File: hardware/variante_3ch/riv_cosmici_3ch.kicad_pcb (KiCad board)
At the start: 2 copper layers, 103 x 215 mm, 203 parts, among them J101 SiPM_CH1, J104 LEMO_CH1, J201 SiPM_CH2, J204 LEMO_CH2, J3 PWR_5V, J301 SiPM_CH3, J304 LEMO_CH3, J5 LEMO_AND, J6 I2C_RPI, Q101 BFR93A, Q102 MMBTH81, Q201 BFR93A, Q202 MMBTH81, Q301 BFR93A, Q302 MMBTH81, U1 LT3461, U10 74LVC1G11, U102 TLC555/LMC555, U103 MAX961, U108 LT1636, U109 74LVC1G17, U11 MCP3424, U202 TLC555/LMC555, U203 MAX961, U208 LT1636, U209 74LVC1G17, U302 TLC555/LMC555, U303 MAX961, U308 LT1636, U309 74LVC1G17, U5 LP2985AIM5-3.6, U6 MCP1825S-3302, U7 LP2985AIM5-3.6

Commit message: KiCad 10: nomi delle reti del PCB allineati allo schema, VOUT del LT3461 come uscita di alimentazione
- allinea_reti_kicad.py (chiamato da gen_variante3): le reti del PCB prendono i nomi
  che KiCad ricava dallo schema (/ETICHETTA, Net-(...), unconnected-(...)), dopo aver
  verificato che i collegamenti coincidono: elimina i 199 net_conflict del DRC con
  --schematic-parity.
- LT3461 pin 5 (CAP/VOUT) di tipo power_out: risolve l'unico power_pin_not_driven
  dell'ERC (VOUT40 alimenta i V+ dei tre LT1636).
Verifica KiCad su entrambe le schede: OK.

Co-Authored-By: Claude Opus 5.5 <noreply@anthropic.com>
Claude-Session: https://claude.ai/code/session_017fc9yPsNewCQrMK8R1c8Ls
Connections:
- net AND_IN1 renamed /AND_IN1
- net AND_IN2 renamed /AND_IN2
- net AND_IN3 renamed /AND_IN3
- net AND_OUT renamed /AND_OUT
- net AND_Y renamed /AND_Y
- net BIAS1 renamed /BIAS1
- net BIAS2 renamed /BIAS2
- net BIAS3 renamed /BIAS3
- net BUF_OUT1 renamed Net-(J104-Pad1)
- net BUF_OUT2 renamed Net-(J204-Pad1)
- net BUF_OUT3 renamed Net-(J304-Pad1)
- net BUF_Y1 renamed /BUF_Y1
- net BUF_Y2 renamed /BUF_Y2
- net BUF_Y3 renamed /BUF_Y3
- net CMP_IN1 renamed /CMP_IN1
- net CMP_IN2 renamed /CMP_IN2
- net CMP_IN3 renamed /CMP_IN3
- net CMP_Q1 renamed /CMP_Q1
- net CMP_Q2 renamed /CMP_Q2
- net CMP_Q3 renamed /CMP_Q3
- net CMP_QB1 renamed /CMP_QB1
- net CMP_QB2 renamed /CMP_QB2
- net CMP_QB3 renamed /CMP_QB3
- net CTL5551 renamed Net-(U102-CTL)
- net CTL5552 renamed Net-(U202-CTL)
- net CTL5553 renamed Net-(U302-CTL)
- net FB renamed Net-(U1-FB)
- net I2C_SCL renamed /I2C_SCL
- net I2C_SDA renamed /I2C_SDA
- net INV1 renamed Net-(U108--)
- net INV2 renamed Net-(U208--)
- net INV3 renamed Net-(U308--)
- net LE1 renamed Net-(U103-LE)
- net LE2 renamed Net-(U203-LE)
- net LE3 renamed Net-(U303-LE)
- net LED_A1 renamed Net-(U102-Q)
- net LED_A2 renamed Net-(U202-Q)
- net LED_A3 renamed Net-(U302-Q)
- net LED_K1 renamed Net-(D103-A)
- net LED_K2 renamed Net-(D203-A)
- net LED_K3 renamed Net-(D303-A)
- net MON1 renamed /MON1
- net MON2 renamed /MON2
- net MON3 renamed /MON3
- net MON4 renamed /MON4
- net Q1B1 renamed Net-(Q101-B)
- net Q1B2 renamed Net-(Q201-B)
- net Q1B3 renamed Net-(Q301-B)
- net Q1C1 renamed Net-(Q101-C)
- net Q1C2 renamed Net-(Q201-C)
- net Q1C3 renamed Net-(Q301-C)
- net Q2C1 renamed Net-(Q102-C)
- net Q2C2 renamed Net-(Q202-C)
- net Q2C3 renamed Net-(Q302-C)
- net Q2E1 renamed Net-(Q102-E)
- net Q2E2 renamed Net-(Q202-E)
- net Q2E3 renamed Net-(Q302-E)
- net SCL_ADC renamed /SCL_ADC
- net SDA_ADC renamed /SDA_ADC
- net SIG_IN1 renamed /SIG_IN1
- net SIG_IN2 renamed /SIG_IN2
- net SIG_IN3 renamed /SIG_IN3
- net SW renamed Net-(U1-SW)
- net T5551 renamed Net-(U102-DIS)
- net T5552 renamed Net-(U202-DIS)
- net T5553 renamed Net-(U302-DIS)
- net TH1 renamed /TH1
- net TH2 renamed /TH2
- net TH3 renamed /TH3
- net TH_HI1 renamed Net-(R119-Pad1)
- net TH_HI2 renamed Net-(R219-Pad1)
- net TH_HI3 renamed Net-(R319-Pad1)
- net TH_LO1 renamed Net-(R118-Pad1)
- net TH_LO2 renamed Net-(R218-Pad1)
- net TH_LO3 renamed Net-(R318-Pad1)
- net TH_W1 renamed Net-(V102-W)
- net TH_W2 renamed Net-(V202-W)
- net TH_W3 renamed Net-(V302-W)
- net VADJ_HI1 renamed Net-(D101-K)
- net VADJ_HI2 renamed Net-(D201-K)
- net VADJ_HI3 renamed Net-(D301-K)
- net VADJ_LO1 renamed Net-(R107-Pad1)
- net VADJ_LO2 renamed Net-(R207-Pad1)
- net VADJ_LO3 renamed Net-(R307-Pad1)
- net VOUT40 renamed /VOUT40
- net VREF_B renamed /VREF_B
- net VREG381 renamed /VREG381
- net VREG382 renamed /VREG382
- net VREG383 renamed /VREG383
- net VSET1 renamed Net-(U108-+)
- net VSET2 renamed Net-(U208-+)
- net VSET3 renamed Net-(U308-+)
- U108 pad 1: (no net) -> unconnected-(U108-NC-Pad1)
- U108 pad 5: (no net) -> unconnected-(U108-NC-Pad5)
- U108 pad 8: (no net) -> unconnected-(U108-NC-Pad8)
- U109 pad 1: (no net) -> unconnected-(U109-NC-Pad1)
- U208 pad 1: (no net) -> unconnected-(U208-NC-Pad1)
- U208 pad 5: (no net) -> unconnected-(U208-NC-Pad5)
- U208 pad 8: (no net) -> unconnected-(U208-NC-Pad8)
- U209 pad 1: (no net) -> unconnected-(U209-NC-Pad1)
- U308 pad 1: (no net) -> unconnected-(U308-NC-Pad1)
- U308 pad 5: (no net) -> unconnected-(U308-NC-Pad5)
- U308 pad 8: (no net) -> unconnected-(U308-NC-Pad8)
- U309 pad 1: (no net) -> unconnected-(U309-NC-Pad1)
- U5 pad 4: (no net) -> unconnected-(U5-BYP-Pad4)
- U7 pad 4: (no net) -> unconnected-(U7-BYP-Pad4)

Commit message: R3 = 255k e 2,2 uF su CF4/CF7/CF9 (datasheet LT3461, LP2985, MCP1825), nota per la verifica INFN
- R3 270k -> 255k: VOUT40 da 41,7 a 39,4 V, sotto i 40 V max assoluti del LT3461;
  bias ancora regolabile fino a ~39,2 V (margine 1,0 V a 25 C, 0,3 V a 50 C).
- CF4, CF7, CF9 100n -> 2,2 uF X7R 0805 (Samsung CL21B225KAFNNNE): uscite dei
  regolatori, come richiesto dai datasheet.
- Schemi, PCB (valori), BOM, file JLCPCB, PDF, simulazioni e render rigenerati;
  verifica_ltspice: tutto OK; sim_3canali invariata salvo VOUT40.
- hardware/variante_3ch/NOTA_PER_TECNICO_INFN.txt: le due modifiche con calcoli,
  simulazioni e punti da verificare, piu' l'elenco delle differenze dalla scheda INFN.

Co-Authored-By: Claude Opus 5.5 <noreply@anthropic.com>
Claude-Session: https://claude.ai/code/session_017fc9yPsNewCQrMK8R1c8Ls
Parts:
- CF4, CF7, CF9: value 100n -> 2.2uF
- R3: value 270k -> 255k

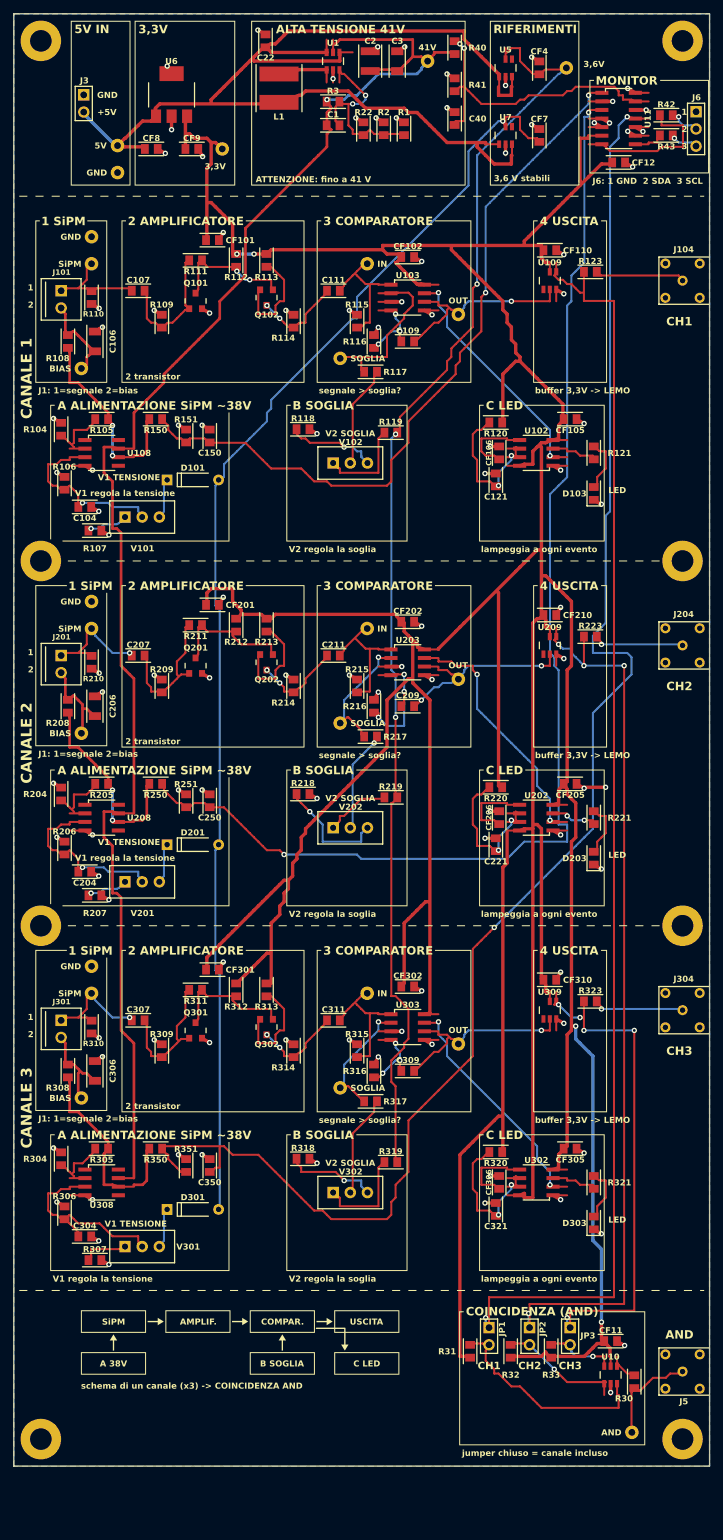
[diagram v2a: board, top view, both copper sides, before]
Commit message: Monitor: J6 Molex KK 254 a 3 poli (22-27-2031) come i connettori delle barre
Footprint MOLEX_KK_3, J6 spostato in orizzontale nel blocco MONITOR (il corpo del KK
sporgeva dal bordo); ri-instradate solo I2C_SDA e I2C_SCL (reinstrada_reti3.py),
resto del routing invariato. DRC 0, connettivita' OK, verifica KiCad OK.
Lista Mouser: 22-27-2031 x3, 22-01-3037 x3, contatti 08-50-0114 x30.
Serigrafia, Gerber, JLCPCB, PDF, zip KiCad, modello 3D e render aggiornati.

Co-Authored-By: Claude Opus 5.5 <noreply@anthropic.com>
Claude-Session: https://claude.ai/code/session_017fc9yPsNewCQrMK8R1c8Ls
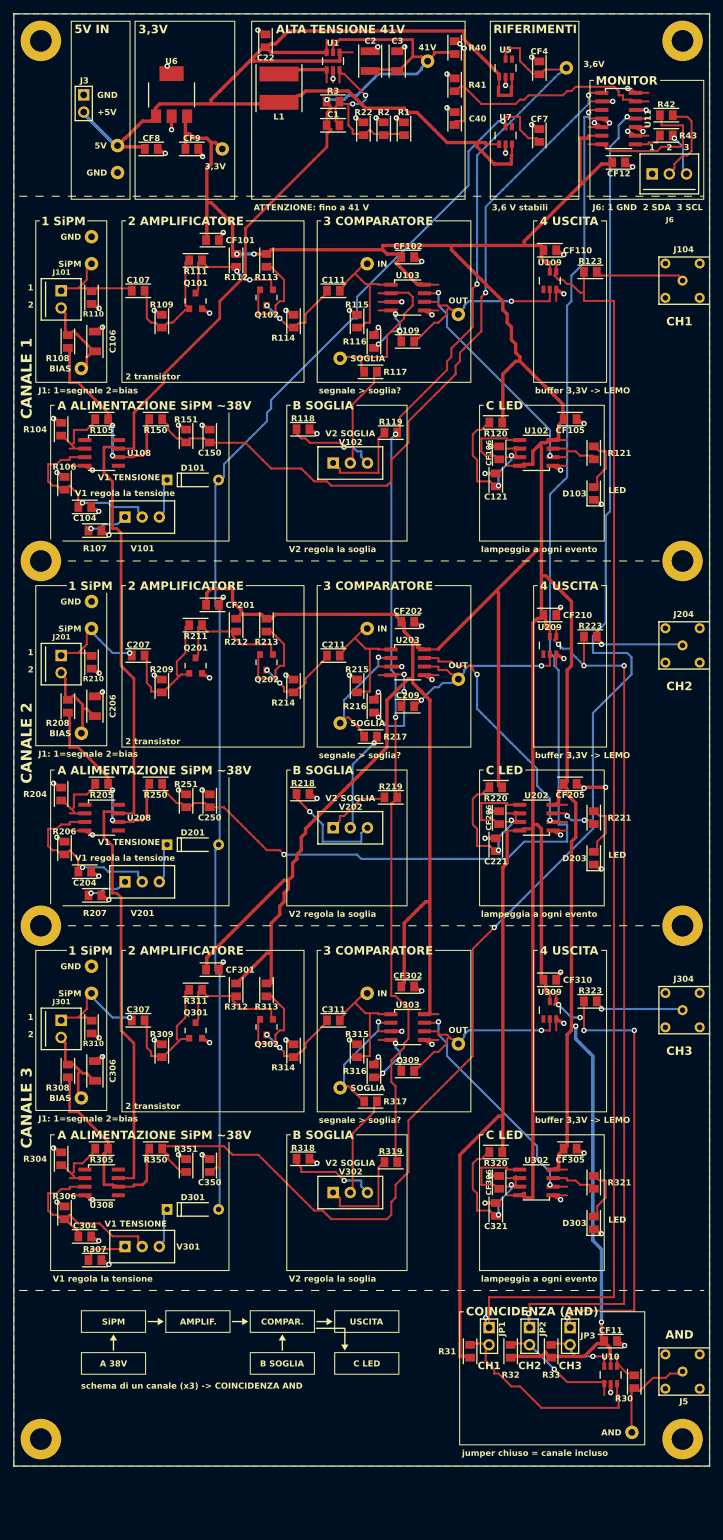
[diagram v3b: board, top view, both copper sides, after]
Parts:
- J6: footprint rivlib:HDR1x03 -> rivlib:MOLEX_KK_3
- moved J6 11.3 mm to (114.5, 43.7), turned to 0 degrees
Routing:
- net /I2C_SDA: track 4.58 -> 12.6 mm, vias 1 -> 0
- net /I2C_SCL: track 3.66 -> 5.96 mm

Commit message: Secondo ADC per soglie e temperatura: PCB a 3 canali rifatto e verificato (103 x 223,9 mm)
- routing completo con il nuovo blocco MONITOR (U11 + U12 affiancati, termistore, J6)
  e la lettura delle soglie (R?52 10k + C?52 100n accanto al pin 2 del comparatore):
  0 reti fallite, DRC 0, connettivita' OK; verifica KiCad: schema = PCB, nessun errore,
  0 reti spezzate sul rame reale.
- regola di distanza piste del monitor <-> nodi sensibili resa simmetrica (1,2 mm su
  entrambi gli strati): rifatte Q1B3, Q2C2, MON3 (MON3 fuori dalla zona dell'uscita
  del canale 2, niente isole di massa), CMP_IN2 e MONTH2; ingresso comparatore
  20,6-20,9 mm in tutti e tre i canali, senza vie.
- C11 spostato di 1,27 mm (spazio per le scritte di C52/R52); serigrafia 0805 con i
  trattini tra i pad (niente contorni che si toccano: silk_overlap 0).
- Gerber, JLCPCB (U11+U12 MCP3424, RT1 NCP21XV103J03RA, R44 22k), stampa 1:1, schemi,
  zip KiCad, render rigenerati; tolto l'avviso 'lavoro in corso'.

Co-Authored-By: Claude Opus 5.5 <noreply@anthropic.com>
Claude-Session: https://claude.ai/code/session_017fc9yPsNewCQrMK8R1c8Ls
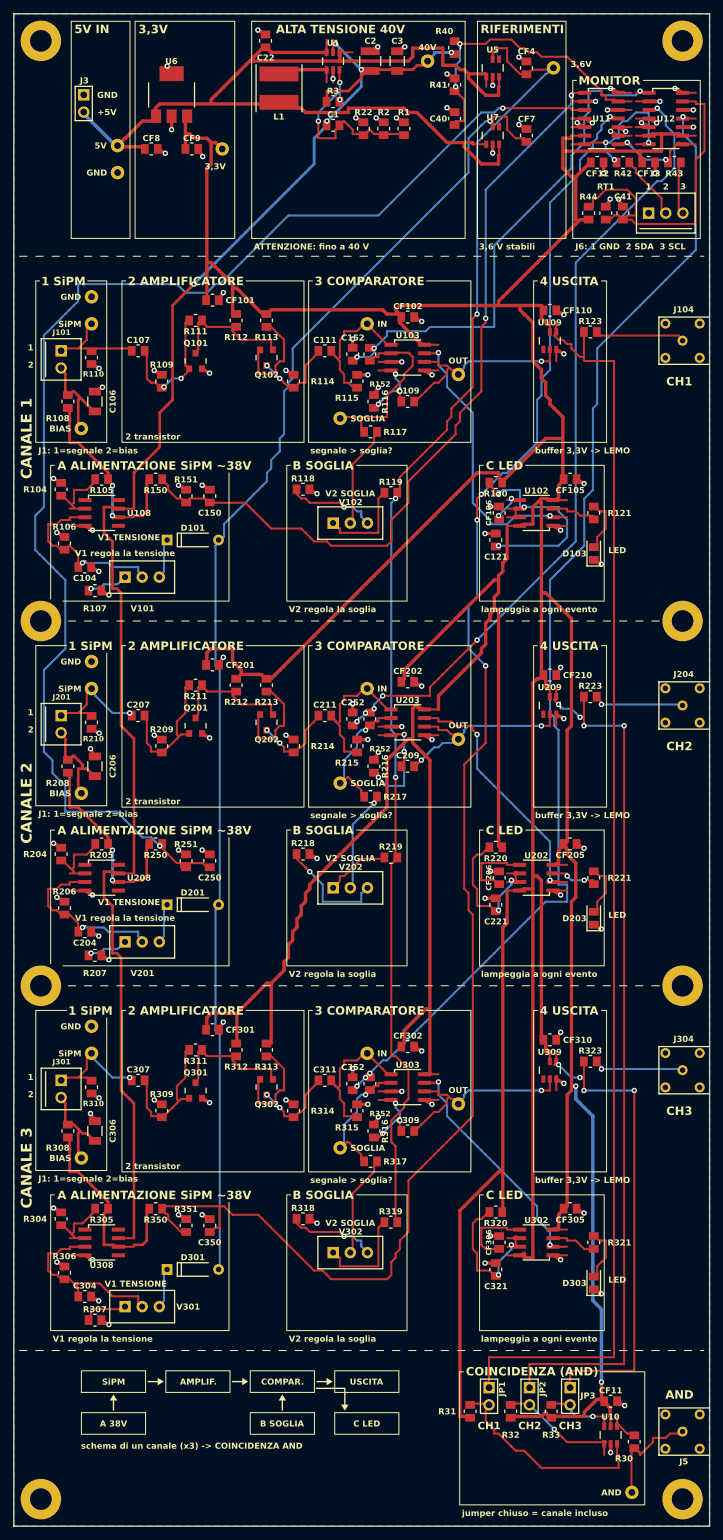
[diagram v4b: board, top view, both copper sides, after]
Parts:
- added C152: 100n, rivlib:C_0805, F.Cu at (70.2, 70.4)
- added C252: 100n, rivlib:C_0805, F.Cu at (70.2, 124.4)
- added C352: 100n, rivlib:C_0805, F.Cu at (70.2, 178.4)
- added C41: 100n, rivlib:C_0805, F.Cu at (110.2, 49.5)
- added CF13: 100n, rivlib:C_0805, F.Cu at (114.0, 42.0)
- added R152: 10k, rivlib:R_0805, F.Cu at (72.7, 70.4)
- added R252: 10k, rivlib:R_0805, F.Cu at (72.7, 124.4)
- added R352: 10k, rivlib:R_0805, F.Cu at (72.7, 178.4)
- added R44: 22k, rivlib:R_0805, F.Cu at (105.1, 49.5)
- added RT1: 10k NTC, rivlib:R_0805, F.Cu at (107.6, 49.5)
- added U12: MCP3424, rivlib:SOIC14, F.Cu at (116.5, 35.5)
- moved R42 9.50 mm to (110.2, 42.0)
- moved C111 8.98 mm to (66.0, 69.9)
- moved C211 8.98 mm to (66.0, 123.9)
- moved C311 8.98 mm to (66.0, 177.9)
- moved R323 8.89 mm to (105.3, 175.1)
- moved C104 8.89 mm to (30.5, 101.9)
- moved C106 8.89 mm to (32.0, 77.4)
- moved C107 8.89 mm to (38.4, 69.9)
- moved C109 8.89 mm to (78.3, 77.4)
- moved C121 8.89 mm to (91.3, 97.9)
- moved C150 8.89 mm to (49.0, 91.4)
- moved C207 8.89 mm to (38.4, 123.9)
- moved CF101 8.89 mm to (49.4, 62.4)
- moved CF102 8.89 mm to (78.3, 64.9)
- moved CF105 8.89 mm to (102.3, 88.9)
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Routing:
- net /MONTH3: track 0.00 -> 174.2 mm, vias 0 -> 4
- net /MONTH2: track 0.00 -> 117.6 mm, vias 0 -> 6
- net +3V3: track 840.6 -> 940.9 mm, vias 4 -> 2
- net /MONTH1: track 0.00 -> 75.5 mm, vias 0 -> 3
- net /MONT: track 0.00 -> 49.9 mm
- net GND: track 201.1 -> 225.2 mm, vias 106 -> 117
- net /MON2: track 181.1 -> 200.8 mm
- net +5V: track 170.4 -> 157.8 mm
- net /SCL_ADC: track 4.56 -> 16.0 mm, vias 0 -> 2
- net Net-(U102-DIS): track 25.8 -> 36.6 mm, vias 2 -> 3
- net +3V6: track 189.8 -> 199.1 mm
- net /MON1: track 110.5 -> 118.3 mm
- net /VREF_B: track 190.2 -> 198.0 mm
- net /CMP_QB1: track 36.1 -> 43.2 mm
- net Net-(U102-CTL): track 10.7 -> 6.37 mm, vias 0 -> 2
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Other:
- board size 103 x 215 mm -> 103 x 223.9 mm
